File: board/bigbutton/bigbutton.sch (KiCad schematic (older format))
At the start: 55 parts, among them J1 SWD, J2 USB_C_Receptacle_USB2.0, SW1 RESET, SW2 SMOL, SW3 LORGE, U1 STM32F302CBTx, U2 ATECC608A-SSHDA, U3 WE-TVS-82400102, X1 16MHz

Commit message: Start PCB routing
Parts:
- C20, C21: renamed from C?; footprint (none) -> Capacitor_SMD:C_0603_1608Metric_Pad1.05x0.95mm_HandSolder
- J1: footprint (none) -> Connector_PinHeader_1.27mm:PinHeader_2x05_P1.27mm_Vertical
- J2: footprint (none) -> bigbutton:USB_C_Receptacle_HRO_TYPE-C-31-M-13_handsolder
- SW1: footprint (none) -> bigbutton:SW_SPST_XKB_TS-1187A
- SW2: footprint Button_Switch_Keyboard:SW_Cherry_MX_1.00u_PC -> Button_Switch_Keyboard:SW_Cherry_MX_1.00u_PCB
- SW3: footprint Button_Switch_Keyboard:SW_Cherry_MX_1.00u_PC -> bigbutton:SW_BIG_SWITCH
- TP_3V3_1, TP_5V_1, TP_CC1_1, TP_CC2_1, TP_D+_1, TP_D-_1, TP_GND_1, TP_SCL_1, TP_SDA_1, TP_~RST~_1: footprint (none) -> TestPoint:TestPoint_Pad_D1.0mm
- U3: value WE-TVS-82400102 -> USBLC6-2; footprint Package_TO_SOT_SMD:SOT-23-6 -> Package_TO_SOT_SMD:SOT-23-6_Handsoldering
- U4: renamed from U?; footprint Package_TO_SOT_SMD:SOT-23-5 -> Package_TO_SOT_SMD:SOT-23-5_HandSoldering
- U5: renamed from U?; value MIC5501-3.3YM5 -> MIC5504-3.3YM5; footprint Package_TO_SOT_SMD:SOT-23-5 -> Package_TO_SOT_SMD:SOT-23-5_HandSoldering
- X1: footprint (none) -> Crystal:Resonator-2Pin_W8.0mm_H3.5mm
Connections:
- net USB_UNFILTERED_D+: now reaches J2.A6 (D+), J2.B6 (D+), U3.3
- net USB_UNFILTERED_D-: now reaches J2.A7 (D-), J2.B7 (D-), U3.1
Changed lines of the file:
@@
 F 0 "X1" V 2950 2350 50  0000 L CNN
 F 1 "16MHz" V 2850 2250 50  0000 L CNN
-F 2 "" H 2900 2600 50  0001 C CNN
+F 2 "Crystal:Resonator-2Pin_W8.0mm_H3.5mm" H 2900 2600 50  0001 C CNN
 F 3 "~" H 2900 2600 50  0001 C CNN
 	1    2900 2600
@@
 F 0 "J1" H 707 1396 50  0000 R CNN
 F 1 "SWD" H 707 1305 50  0000 R CNN
-F 2 "" H 1150 1350 50  0001 C CNN
+F 2 "Connector_PinHeader_1.27mm:PinHeader_2x05_P1.27mm_Vertical" H 1150 1350 50  0001 C CNN
 F 3 "http://infocenter.arm.com/help/topic/com.arm.doc.ddi0314h/DDI0314H_coresight_components_trm.pdf" V 800 100 50  0001 C CNN
 	1    1150 1350
@@
 Wire Wire Line
 	1350 7100 1350 7000
-$Comp
-L Power_Protection:WE-TVS-82400102 U3
-U 1 1 5F6430C8
-P 3150 6100
-F 0 "U3" H 3150 6425 50  0000 C CNN
-F 1 "WE-TVS-82400102" H 3150 6334 50  0000 C CNN
-F 2 "Package_TO_SOT_SMD:SOT-23-6" H 3150 5900 50  0001 C CNN
-F 3 "https://katalog.we-online.de/pbs/datasheet/82400102.pdf" H 3150 5850 50  0001 C CNN
-	1    3150 6100
-	1    0    0    -1
-$EndComp
 Wire Wire Line
 	1950 6000 2850 6000
@@
 F 0 "J2" H 1457 6967 50  0000 C CNN
 F 1 "USB_C_Receptacle_USB2.0" H 1457 6876 50  0000 C CNN
-F 2 "" H 1500 6100 50  0001 C CNN
+F 2 "bigbutton:USB_C_Receptacle_HRO_TYPE-C-31-M-13_handsolder" H 1500 6100 50  0001 C CNN
 F 3 "https://www.usb.org/sites/default/files/documents/usb_type-c.zip" H 1500 6100 50  0001 C CNN
 	1    1350 6100
@@
 F 0 "SW2" H 5800 3450 50  0000 C CNN
 F 1 "SMOL" H 5800 3350 50  0000 C CNN
-F 2 "Button_Switch_Keyboard:SW_Cherry_MX_1.00u_PC" H 5600 3450 50  0001 C CNN
+F 2 "Button_Switch_Keyboard:SW_Cherry_MX_1.00u_PCB" H 5600 3450 50  0001 C CNN
 F 3 "~" H 5600 3450 50  0001 C CNN
 	1    5600 3250
@@
 F 0 "SW1" H 2600 1685 50  0000 C CNN
 F 1 "RESET" H 2600 1594 50  0000 C CNN
-F 2 "" H 2600 1600 50  0001 C CNN
+F 2 "bigbutton:SW_SPST_XKB_TS-1187A" H 2600 1600 50  0001 C CNN
 F 3 "~" H 2600 1600 50  0001 C CNN
 	1    2600 1400
@@
 F 0 "SW3" H 5800 3750 50  0000 C CNN
 F 1 "LORGE" H 5850 3650 50  0000 C CNN
-F 2 "Button_Switch_Keyboard:SW_Cherry_MX_1.00u_PC" H 5600 3750 50  0001 C CNN
+F 2 "bigbutton:SW_BIG_SWITCH" H 5600 3750 50  0001 C CNN
 F 3 "~" H 5600 3750 50  0001 C CNN
 	1    5600 3550
@@
 F 0 "TP_~RST~_1" V 3250 2500 50  0000 C CNN
 F 1 "TestPoint" V 3354 2222 50  0001 C CNN
-F 2 "" H 3450 2150 50  0001 C CNN
+F 2 "TestPoint:TestPoint_Pad_D1.0mm" H 3450 2150 50  0001 C CNN
 F 3 "~" H 3450 2150 50  0001 C CNN
 	1    3250 2150
@@
 F 0 "TP_CC2_1" H 1900 5800 25  0000 L CNN
 F 1 "TP_CC2" H 1998 5805 25  0001 L CNN
-F 2 "" H 2150 5850 50  0001 C CNN
+F 2 "TestPoint:TestPoint_Pad_D1.0mm" H 2150 5850 50  0001 C CNN
 F 3 "~" H 2150 5850 50  0001 C CNN
 	1    1950 5850
@@
 F 0 "TP_CC1_1" H 1900 5650 25  0000 L CNN
 F 1 "TP_CC1" H 1950 5650 25  0001 L CNN
-F 2 "" H 2150 5600 50  0001 C CNN
+F 2 "TestPoint:TestPoint_Pad_D1.0mm" H 2150 5600 50  0001 C CNN
 F 3 "~" H 2150 5600 50  0001 C CNN
 	1    1950 5600
@@
 F 0 "TP_SCL_1" H 5198 4150 50  0000 L CNN
 F 1 "TestPoint_Small" H 5198 4105 50  0001 L CNN
-F 2 "" H 5350 4150 50  0001 C CNN
+F 2 "TestPoint:TestPoint_Pad_D1.0mm" H 5350 4150 50  0001 C CNN
 F 3 "~" H 5350 4150 50  0001 C CNN
 	1    5150 4150
@@
 F 0 "TP_SDA_1" H 5198 4250 50  0000 L CNN
 F 1 "TestPoint_Small" H 5198 4205 50  0001 L CNN
-F 2 "" H 5350 4250 50  0001 C CNN
+F 2 "TestPoint:TestPoint_Pad_D1.0mm" H 5350 4250 50  0001 C CNN
 F 3 "~" H 5350 4250 50  0001 C CNN
 	1    5150 4250
@@
 F 0 "TP_D-_1" H 5198 4350 50  0000 L CNN
 F 1 "TestPoint_Small" H 5198 4305 50  0001 L CNN
-F 2 "" H 5350 4350 50  0001 C CNN
+F 2 "TestPoint:TestPoint_Pad_D1.0mm" H 5350 4350 50  0001 C CNN
 F 3 "~" H 5350 4350 50  0001 C CNN
 	1    5150 4350
@@
 F 0 "TP_D+_1" H 5198 4450 50  0000 L CNN
 F 1 "TestPoint_Small" H 5198 4405 50  0001 L CNN
-F 2 "" H 5350 4450 50  0001 C CNN
+F 2 "TestPoint:TestPoint_Pad_D1.0mm" H 5350 4450 50  0001 C CNN
 F 3 "~" H 5350 4450 50  0001 C CNN
 	1    5150 4450
@@
 	6400 2200 6900 2200
 $Comp
-L bigbutton:SN74LV1T34DBV U?
+L bigbutton:SN74LV1T34DBV U4
 U 1 1 5F7A4DA0
 P 6050 2200
-F 0 "U?" H 5850 2600 50  0000 L CNN
+F 0 "U4" H 5850 2600 50  0000 L CNN
 F 1 "SN74LV1T34DBV" H 5350 2500 50  0000 L CNN
-F 2 "Package_TO_SOT_SMD:SOT-23-5" H 6050 1450 50  0001 C CNN
+F 2 "Package_TO_SOT_SMD:SOT-23-5_HandSoldering" H 6050 1450 50  0001 C CNN
 F 3 "https://www.ti.com/lit/ds/symlink/sn74lv1t34.pdf" H 5100 1750 50  0001 C CNN
 	1    6050 2200
@@
 MCU_DOUT
 $Comp
-L power:GND #PWR?
+L power:GND #PWR03
 U 1 1 5F7A7DA0
 P 6050 2550
-F 0 "#PWR?" H 6050 2300 50  0001 C CNN
+F 0 "#PWR03" H 6050 2300 50  0001 C CNN
 F 1 "GND" H 6055 2377 50  0000 C CNN
 F 2 "" H 6050 2550 50  0001 C CNN
@@
 $EndComp
 $Comp
-L power:+5V #PWR?
+L power:+5V #PWR01
 U 1 1 5F7A86E9
 P 6050 1850
-F 0 "#PWR?" H 6050 1700 50  0001 C CNN
+F 0 "#PWR01" H 6050 1700 50  0001 C CNN
 F 1 "+5V" H 6065 2023 50  0000 C CNN
 F 2 "" H 6050 1850 50  0001 C CNN
@@
 	1    0    0    -1
 $EndComp
-$Comp
-L Regulator_Linear:MIC5501-3.0YM5 U?
-U 1 1 5F7ACD40
-P 5100 6500
-F 0 "U?" H 5100 6867 50  0000 C CNN
-F 1 "MIC5501-3.3YM5" H 5100 6776 50  0000 C CNN
-F 2 "Package_TO_SOT_SMD:SOT-23-5" H 5100 6100 50  0001 C CNN
-F 3 "http://ww1.microchip.com/downloads/en/DeviceDoc/MIC550X.pdf" H 4850 6750 50  0001 C CNN
-	1    5100 6500
-	1    0    0    -1
-$EndComp
 Wire Wire Line
 	4700 6400 4700 6600
@@
 Connection ~ 4700 6400
 $Comp
-L power:+5V #PWR?
+L power:+5V #PWR09
 U 1 1 5F7B4962
 P 4500 6300
-F 0 "#PWR?" H 4500 6150 50  0001 C CNN
+F 0 "#PWR09" H 4500 6150 50  0001 C CNN
 F 1 "+5V" H 4515 6473 50  0000 C CNN
 F 2 "" H 4500 6300 50  0001 C CNN
@@
 	5700 6400 5700 6300
 $Comp
-L power:+3V3 #PWR?
+L power:+3V3 #PWR034
 U 1 1 5F7B7EC3
 P 5700 6300
-F 0 "#PWR?" H 5700 6150 50  0001 C CNN
+F 0 "#PWR034" H 5700 6150 50  0001 C CNN
 F 1 "+3V3" H 5715 6473 50  0000 C CNN
 F 2 "" H 5700 6300 50  0001 C CNN
@@
 $EndComp
 $Comp
-L power:GND #PWR?
+L power:GND #PWR035
 U 1 1 5F7B8883
 P 5100 6800
-F 0 "#PWR?" H 5100 6550 50  0001 C CNN
+F 0 "#PWR035" H 5100 6550 50  0001 C CNN
 F 1 "GND" H 5105 6627 50  0000 C CNN
 F 2 "" H 5100 6800 50  0001 C CNN
@@
 $EndComp
 $Comp
-L Device:C_Small C?
+L Device:C_Small C20
 U 1 1 5F7B9C07
 P 4500 6500
-F 0 "C?" H 4300 6550 50  0000 L CNN
+F 0 "C20" H 4300 6550 50  0000 L CNN
 F 1 "1µF" H 4250 6450 50  0000 L CNN
-F 2 "" H 4500 6500 50  0001 C CNN
+F 2 "Capacitor_SMD:C_0603_1608Metric_Pad1.05x0.95mm_HandSolder" H 4500 6500 50  0001 C CNN
 F 3 "~" H 4500 6500 50  0001 C CNN
 	1    4500 6500
@@
 	5700 6800 5700 6600
 $Comp
-L Device:C_Small C?
+L Device:C_Small C21
 U 1 1 5F7C0E99
 P 5700 6500
-F 0 "C?" H 5792 6546 50  0000 L CNN
+F 0 "C21" H 5792 6546 50  0000 L CNN
 F 1 "1µF" H 5792 6455 50  0000 L CNN
-F 2 "" H 5700 6500 50  0001 C CNN
+F 2 "Capacitor_SMD:C_0603_1608Metric_Pad1.05x0.95mm_HandSolder" H 5700 6500 50  0001 C CNN
 F 3 "~" H 5700 6500 50  0001 C CNN
 	1    5700 6500
@@
 F 0 "TP_5V_1" H 4050 6300 50  0000 L CNN
 F 1 "TestPoint_Small" H 4448 6255 50  0001 L CNN
-F 2 "" H 4600 6300 50  0001 C CNN
+F 2 "TestPoint:TestPoint_Pad_D1.0mm" H 4600 6300 50  0001 C CNN
 F 3 "~" H 4600 6300 50  0001 C CNN
 	1    4400 6300
@@
 F 0 "TP_GND_1" H 4548 6900 50  0000 L CNN
 F 1 "TestPoint_Small" H 4548 6855 50  0001 L CNN
-F 2 "" H 4700 6900 50  0001 C CNN
+F 2 "TestPoint:TestPoint_Pad_D1.0mm" H 4700 6900 50  0001 C CNN
 F 3 "~" H 4700 6900 50  0001 C CNN
 	1    4500 6900
@@
 F 0 "TP_3V3_1" H 5848 6300 50  0000 L CNN
 F 1 "TestPoint_Small" H 5848 6255 50  0001 L CNN
-F 2 "" H 6000 6300 50  0001 C CNN
+F 2 "TestPoint:TestPoint_Pad_D1.0mm" H 6000 6300 50  0001 C CNN
 F 3 "~" H 6000 6300 50  0001 C CNN
 	1    5800 6300
@@
 Wire Wire Line
 	5800 6400 5700 6400
+Text Label 1950 6000 0    50   ~ 0
+USB_UNFILTERED_D-
+Text Label 1950 6200 0    50   ~ 0
+USB_UNFILTERED_D+
+$Comp
+L Regulator_Linear:MIC5501-3.0YM5 U5
+U 1 1 5F7ACD40
+P 5100 6500
+F 0 "U5" H 5100 6867 50  0000 C CNN
+F 1 "MIC5504-3.3YM5" H 5100 6776 50  0000 C CNN
+F 2 "Package_TO_SOT_SMD:SOT-23-5_HandSoldering" H 5100 6100 50  0001 C CNN
+F 3 "http://ww1.microchip.com/downloads/en/DeviceDoc/MIC550X.pdf" H 4850 6750 50  0001 C CNN
+	1    5100 6500
+	1    0    0    -1
+$EndComp
+$Comp
+L Power_Protection:WE-TVS-82400102 U3
+U 1 1 5F6430C8
+P 3150 6100
+F 0 "U3" H 3150 6425 50  0000 C CNN
+F 1 "USBLC6-2" H 3150 6334 50  0000 C CNN
+F 2 "Package_TO_SOT_SMD:SOT-23-6_Handsoldering" H 3150 5900 50  0001 C CNN
+F 3 "https://datasheet.lcsc.com/szlcsc/2009030936_MCC-Micro-Commercial-Components-SRL05-TP_C779237.pdf" H 3150 5850 50  0001 C CNN
+	1    3150 6100
+	1    0    0    -1
+$EndComp
 $EndSCHEMATC

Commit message: Done with first routing attempt
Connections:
- net ~RST: now reaches C7.1, J1.10 (~RESET~), R1.2, SW1.2, TP_~RST~_1.1, U1.7 (NRST)
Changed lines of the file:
@@
 	1    0    0    -1
 $EndComp
+Text Label 3250 1400 2    50   ~ 0
+~RST
 $EndSCHEMATC

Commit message: Add BOOT0 button
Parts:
- added R6: 10kΩ, Resistor_SMD:R_0603_1608Metric_Pad1.05x0.95mm_HandSolder, symbol Device:R_Small
- added SW4: BOOT0, bigbutton:SW_SPST_XKB_TS-1187A, symbol Switch:SW_Push
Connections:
- net +3V3: now also SW4.1
- net BOOT0: now also R6.1, SW4.2
- net GND: now also R6.2
- no-connect marks 4 -> 29
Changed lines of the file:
@@
 Text Label 3250 1400 2    50   ~ 0
 ~RST
+NoConn ~ 3500 2850
+NoConn ~ 3500 2950
+NoConn ~ 3500 3050
+NoConn ~ 3500 3250
+NoConn ~ 3500 3350
+NoConn ~ 3500 3450
+NoConn ~ 3500 3550
+NoConn ~ 3500 3650
+NoConn ~ 3500 3750
+NoConn ~ 3500 3850
+NoConn ~ 3500 3950
+NoConn ~ 3500 4050
+NoConn ~ 3500 4150
+NoConn ~ 3500 4250
+NoConn ~ 3500 4350
+NoConn ~ 3500 4450
+NoConn ~ 3500 4550
+NoConn ~ 3500 4650
+NoConn ~ 3500 4750
+NoConn ~ 4800 4750
+NoConn ~ 4800 4050
+NoConn ~ 4800 3650
+NoConn ~ 4800 3750
+NoConn ~ 4800 3850
+NoConn ~ 10500 3550
+$Comp
+L Switch:SW_Push SW4
+U 1 1 5F7620D0
+P 1450 2750
+F 0 "SW4" H 1450 3035 50  0000 C CNN
+F 1 "BOOT0" H 1450 2944 50  0000 C CNN
+F 2 "bigbutton:SW_SPST_XKB_TS-1187A" H 1450 2950 50  0001 C CNN
+F 3 "~" H 1450 2950 50  0001 C CNN
+	1    1450 2750
+	1    0    0    -1
+$EndComp
+$Comp
+L power:+3V3 #PWR0125
+U 1 1 5F76361E
+P 1250 2750
+F 0 "#PWR0125" H 1250 2600 50  0001 C CNN
+F 1 "+3V3" V 1265 2878 50  0000 L CNN
+F 2 "" H 1250 2750 50  0001 C CNN
+F 3 "" H 1250 2750 50  0001 C CNN
+	1    1250 2750
+	0    -1   -1   0
+$EndComp
+$Comp
+L Device:R_Small R6
+U 1 1 5F764235
+P 1650 2850
+F 0 "R6" H 1709 2896 50  0000 L CNN
+F 1 "10kΩ" H 1709 2805 50  0000 L CNN
+F 2 "Resistor_SMD:R_0603_1608Metric_Pad1.05x0.95mm_HandSolder" H 1650 2850 50  0001 C CNN
+F 3 "~" H 1650 2850 50  0001 C CNN
+	1    1650 2850
+	1    0    0    -1
+$EndComp
+$Comp
+L power:GND #PWR0126
+U 1 1 5F764D96
+P 1650 2950
+F 0 "#PWR0126" H 1650 2700 50  0001 C CNN
+F 1 "GND" H 1655 2777 50  0000 C CNN
+F 2 "" H 1650 2950 50  0001 C CNN
+F 3 "" H 1650 2950 50  0001 C CNN
+	1    1650 2950
+	1    0    0    -1
+$EndComp
+Text Label 1650 2750 0    50   ~ 0
+BOOT0
 $EndSCHEMATC

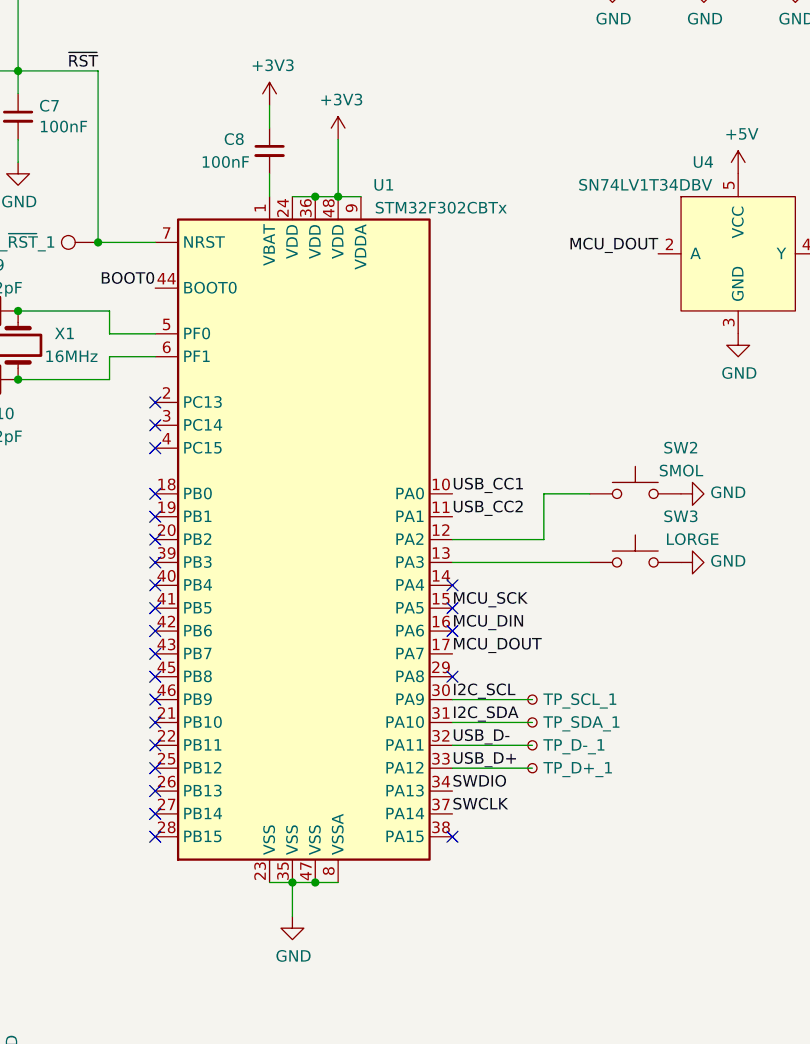
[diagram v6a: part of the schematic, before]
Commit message: Switch to pin-compatible STM32F303CBT6, as reflected in order
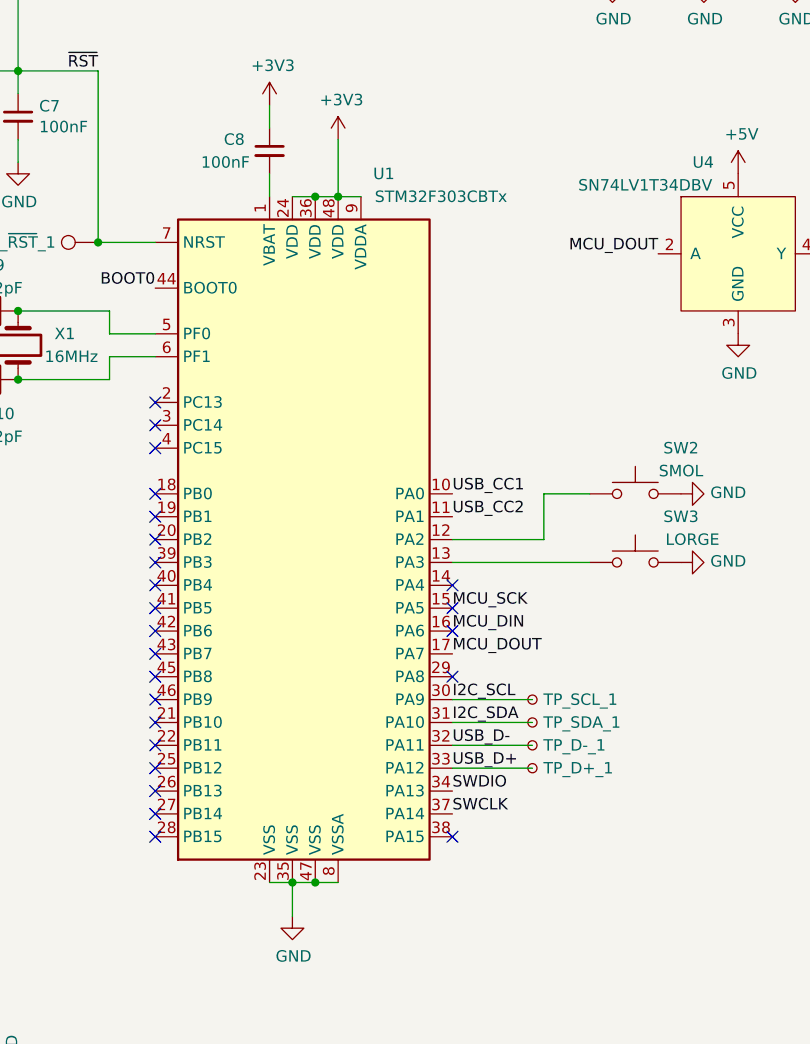
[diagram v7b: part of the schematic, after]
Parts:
- removed U1: STM32F302CBTx, Package_QFP:LQFP-48_7x7mm_P0.5mm, symbol MCU_ST_STM32F3:STM32F302CBTx
- added U1: STM32F303CBTx, Package_QFP:LQFP-48_7x7mm_P0.5mm, symbol MCU_ST_STM32F3:STM32F303CBTx
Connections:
- net +3V3: now also U1.24 (VDD), U1.36 (VDD), U1.48 (VDD), U1.9 (VDDA)
- net BOOT0: now also U1.44 (BOOT0)
- net GND: now also U1.23 (VSS), U1.35 (VSS), U1.47 (VSS), U1.8 (VSSA)
- net I2C_SCL: now also U1.30 (PA9)
- net I2C_SDA: now also U1.31 (PA10)
- net MCU_DIN: now also U1.16 (PA6)
- net MCU_DOUT: now also U1.17 (PA7)
- net MCU_SCK: now also U1.15 (PA5)
- net SWCLK: now also U1.37 (PA14)
- net SWDIO: now also U1.34 (PA13)
- net USB_CC1: now also U1.10 (PA0)
- net USB_CC2: now also U1.11 (PA1)
- net USB_D+: now also U1.33 (PA12)
- net USB_D-: now also U1.32 (PA11)
- net ~RST: now also U1.7 (NRST)
- net at C10.2, X1.1: now also U1.6 (PF1)
- net at C9.2, X1.2: now also U1.5 (PF0)
- net at C8.2: now also U1.1 (VBAT)
- net at SW2.1: now also U1.12 (PA2)
- net at SW3.1: now also U1.13 (PA3)
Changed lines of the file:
@@
 Wire Wire Line
 	1950 5800 2400 5800
-$Comp
-L MCU_ST_STM32F3:STM32F302CBTx U1
-U 1 1 5F636660
-P 4200 3450
-F 0 "U1" H 4500 5000 50  0000 C CNN
-F 1 "STM32F302CBTx" H 4750 4900 50  0000 C CNN
-F 2 "Package_QFP:LQFP-48_7x7mm_P0.5mm" H 3600 2050 50  0001 R CNN
-F 3 "http://www.st.com/st-web-ui/static/active/en/resource/technical/document/datasheet/DM00094064.pdf" H 4200 3450 50  0001 C CNN
-	1    4200 3450
-	1    0    0    -1
-$EndComp
 Text Label 4800 3850 0    50   ~ 0
 MCU_DIN
 Text Label 4800 3750 0    50   ~ 0
 MCU_SCK
-Wire Wire Line
-	4100 1950 4200 1950
-Connection ~ 4200 1950
-Wire Wire Line
-	4200 1950 4300 1950
 Connection ~ 4300 1950
 Wire Wire Line
@@
 	1    0    0    -1
 $EndComp
-Wire Wire Line
-	4300 4950 4200 4950
 Connection ~ 4100 4950
 Wire Wire Line
 	4100 4950 4000 4950
-Connection ~ 4200 4950
-Wire Wire Line
-	4200 4950 4100 4950
 Wire Wire Line
 	4100 4950 4100 5100
@@
 Text Label 1650 2750 0    50   ~ 0
 BOOT0
+$Comp
+L MCU_ST_STM32F3:STM32F303CBTx U1
+U 1 1 5F712979
+P 4200 3450
+F 0 "U1" H 4500 5050 50  0000 C CNN
+F 1 "STM32F303CBTx" H 4750 4950 50  0000 C CNN
+F 2 "Package_QFP:LQFP-48_7x7mm_P0.5mm" H 3600 2050 50  0001 R CNN
+F 3 "http://www.st.com/st-web-ui/static/active/en/resource/technical/document/datasheet/DM00058181.pdf" H 4200 3450 50  0001 C CNN
+	1    4200 3450
+	1    0    0    -1
+$EndComp
+Wire Wire Line
+	4200 1950 4300 1950
+Wire Wire Line
+	4200 4950 4300 4950
+Wire Wire Line
+	4100 1950 4200 1950
+Connection ~ 4200 1950
+Wire Wire Line
+	4100 4950 4200 4950
+Connection ~ 4200 4950
 $EndSCHEMATC

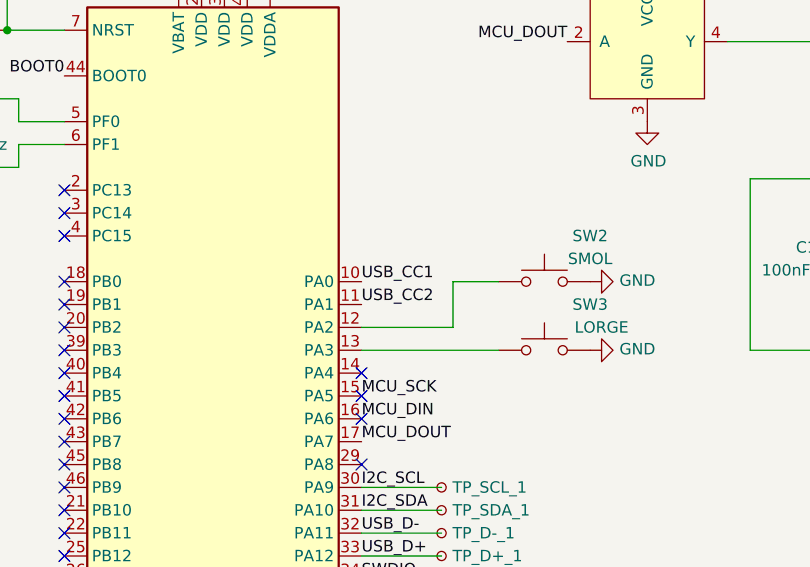
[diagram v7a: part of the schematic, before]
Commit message: Switch to a top-mount USB connector from an incorrect mid-mount
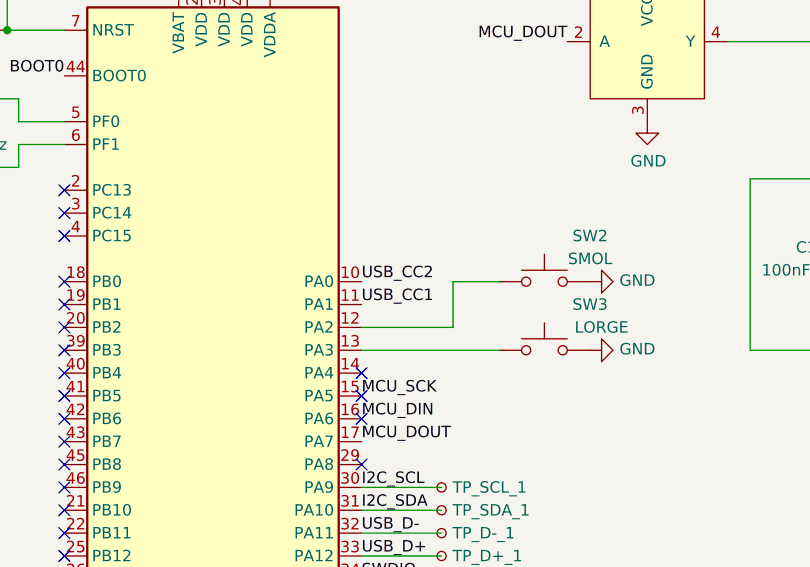
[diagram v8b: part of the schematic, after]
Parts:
- J2: footprint bigbutton:USB_C_Receptacle_HRO_TYPE-C-31-M-13_handsolder -> bigbutton:USB_C_Receptacle_JING_C167321_HandSolder
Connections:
- net USB_CC1: now also U1.11 (PA1); no longer U1.10 (PA0)
- net USB_CC2: now also U1.10 (PA0); no longer U1.11 (PA1)
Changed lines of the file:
@@
 F 0 "J2" H 1457 6967 50  0000 C CNN
 F 1 "USB_C_Receptacle_USB2.0" H 1457 6876 50  0000 C CNN
-F 2 "bigbutton:USB_C_Receptacle_HRO_TYPE-C-31-M-13_handsolder" H 1500 6100 50  0001 C CNN
+F 2 "bigbutton:USB_C_Receptacle_JING_C167321_HandSolder" H 1500 6100 50  0001 C CNN
 F 3 "https://www.usb.org/sites/default/files/documents/usb_type-c.zip" H 1500 6100 50  0001 C CNN
 	1    1350 6100
@@
 Text Label 4800 3950 0    50   ~ 0
 MCU_DOUT
+Text Label 4800 3350 0    50   ~ 0
+USB_CC1
 Text Label 4800 3250 0    50   ~ 0
-USB_CC1
-Text Label 4800 3350 0    50   ~ 0
 USB_CC2
 Text Label 1950 5700 0    50   ~ 0
